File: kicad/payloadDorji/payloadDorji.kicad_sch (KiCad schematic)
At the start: 21 parts, among them J1 Conn_01x01_Pin, J2 Conn_Coaxial, J3 Conn_01x06_Male, U1 LM386, U2 DRA818V, U3 STM32L432KCUx

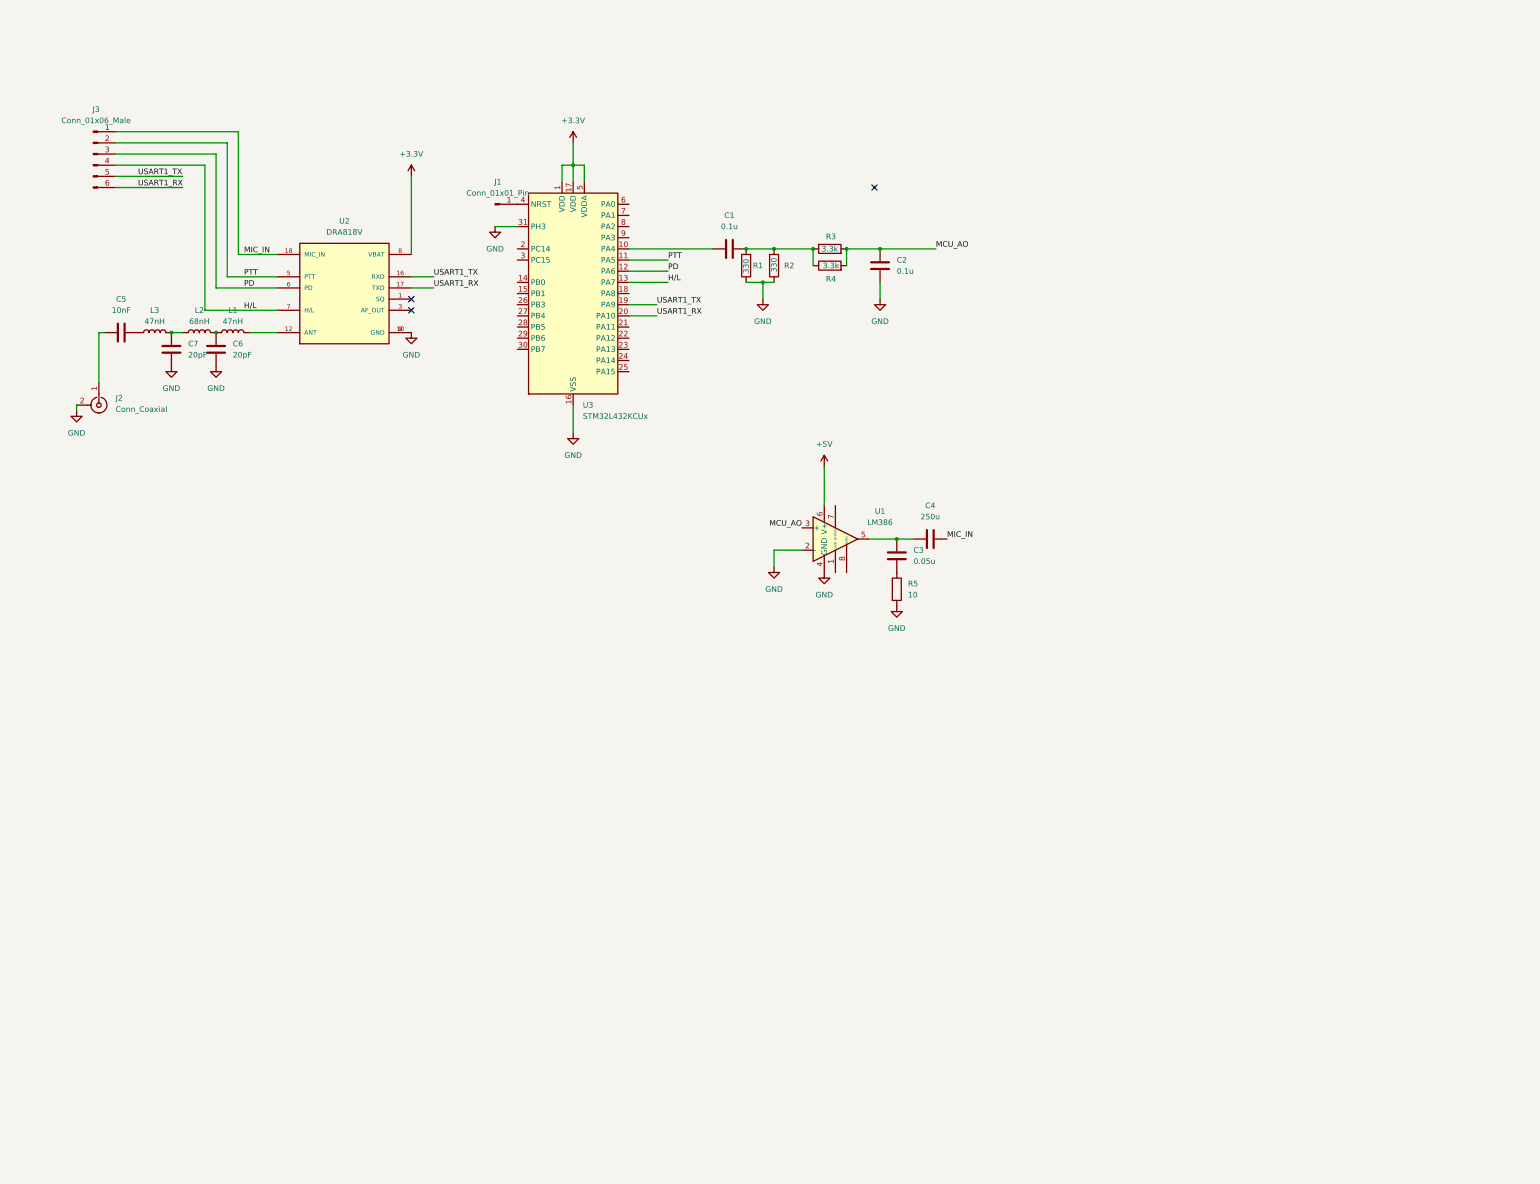
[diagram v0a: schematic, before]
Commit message: payloadDorji add gps and power
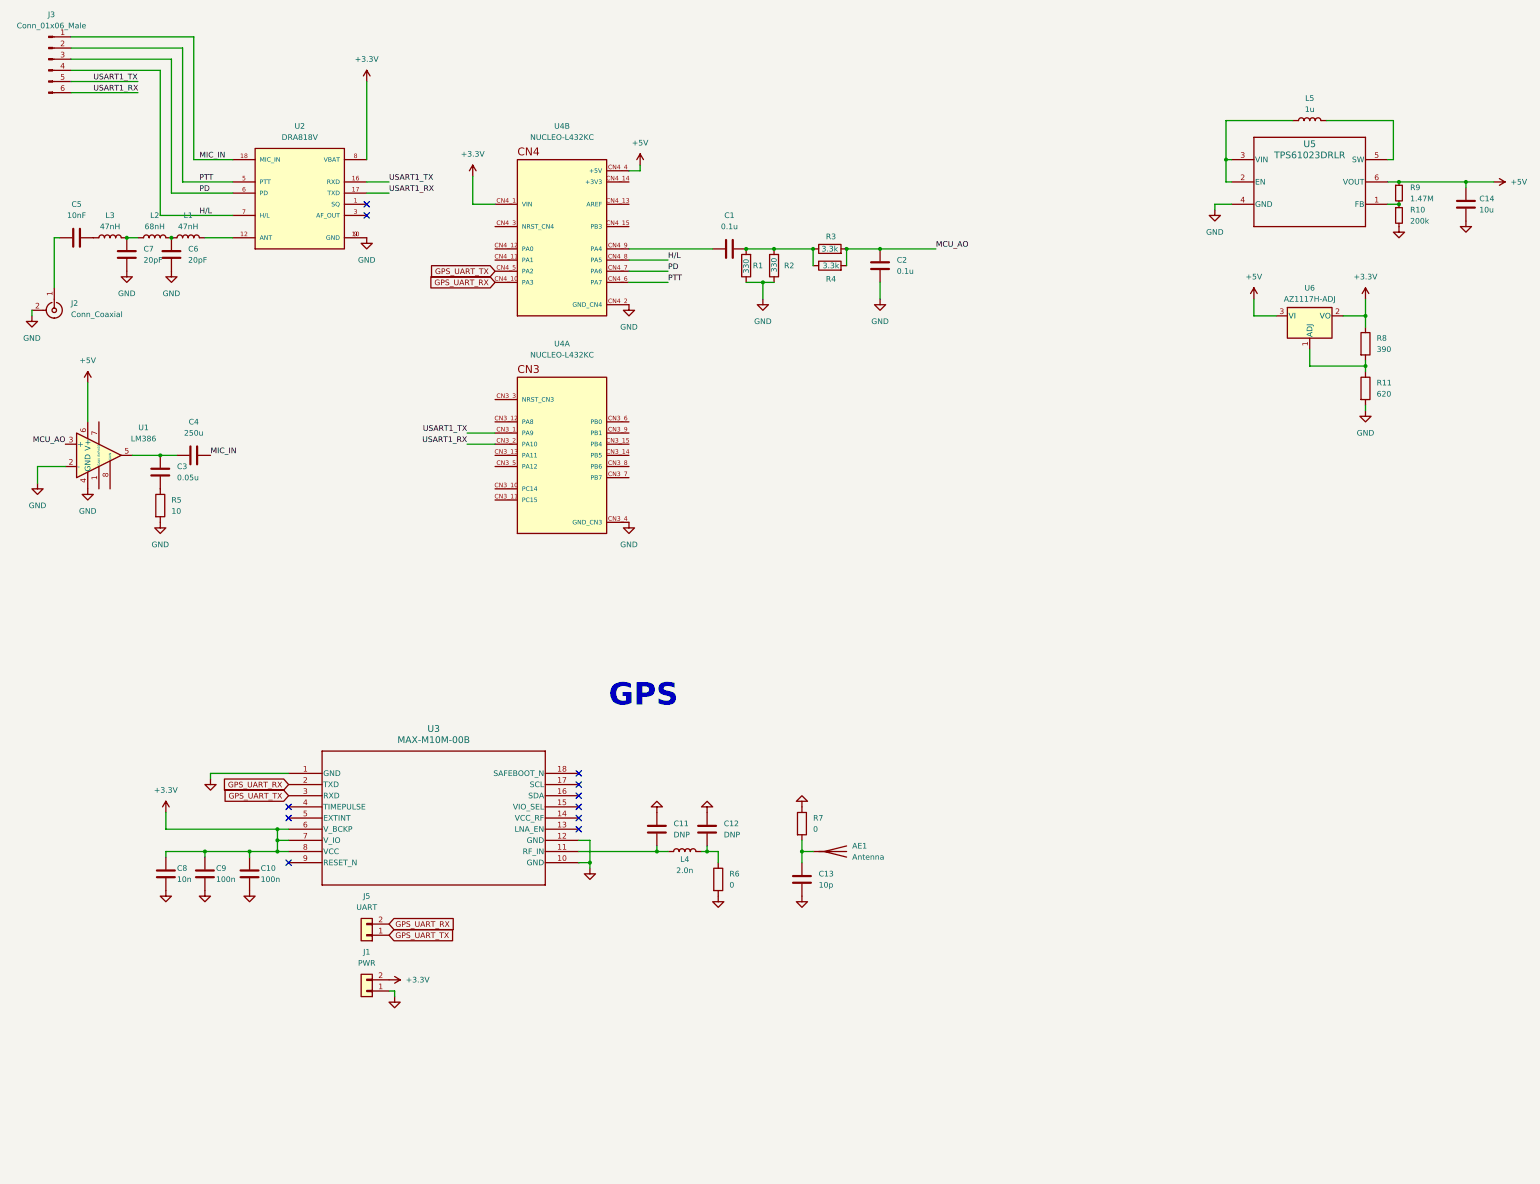
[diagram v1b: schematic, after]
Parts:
- removed J1: Conn_01x01_Pin, Connector_PinSocket_2.54mm:PinSocket_1x01_P2.54mm_Vertical, symbol Connector:Conn_01x01_Pin
- removed U3: STM32L432KCUx, Package_DFN_QFN:QFN-32-1EP_5x5mm_P0.5mm_EP3.45x3.45mm, symbol MCU_ST_STM32L4:STM32L432KCUx
- added AE1: Antenna, PicoAPRS-CustomFootprints:AC30157-01 GNSS Ceramic Chip, symbol Device:Antenna
- added C10, C9: 100n, Capacitor_SMD:C_0402_1005Metric, symbol Device:C
- added C11, C12: DNP, Capacitor_SMD:C_0603_1608Metric, symbol Device:C
- added C13: 10p, Capacitor_SMD:C_0603_1608Metric, symbol Device:C
- added C14: 10u, Capacitor_SMD:C_0603_1608Metric, symbol Device:C
- added C8: 10n, Capacitor_SMD:C_0402_1005Metric, symbol Device:C
- added J1: PWR, Connector_PinHeader_2.54mm:PinHeader_1x02_P2.54mm_Vertical, symbol Connector_Generic:Conn_01x02
- added J5: UART, Connector_PinHeader_2.54mm:PinHeader_1x02_P2.54mm_Vertical, symbol Connector_Generic:Conn_01x02
- added L4: 2.0n, Inductor_SMD:L_0603_1608Metric, symbol Device:L
- added L5: 1u, Inductor_SMD:L_0603_1608Metric, symbol Device:L
- added R10: 200k, Resistor_SMD:R_0603_1608Metric, symbol Device:R_Small
- added R11: 620, symbol Device:R
- added R6, R7: 0, Resistor_SMD:R_0603_1608Metric, symbol Device:R
- added R8: 390, symbol Device:R
- added R9: 1.47M, Resistor_SMD:R_0603_1608Metric, symbol Device:R_Small
- added U3: MAX-M10M-00B, PicoAPRS Custom Parts:MOD18_MAX-M10M_UBL, symbol MAX-M10M:MAX-M10M-00B
- added U4: NUCLEO-L432KC, NUCLEO-L432KC:MODULE_NUCLEO-L432KC, symbol NUCLEO-L432KC:NUCLEO-L432KC
- added U5: TPS61023DRLR, DRL0006A, symbol TPS61023:TPS61023DRLR
- added U6: AZ1117H-ADJ, Package_TO_SOT_SMD:SOT-223-3_TabPin2, symbol Regulator_Linear:AZ1117H-ADJ
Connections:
- net +3.3V: now also C10.1, C8.1, C9.1, J1.2 (Pin_2), R8.1, U3.6 (V_BCKP), U3.7 (V_IO), U3.8 (VCC), U4.CN4_1 (VIN), U6.2 (VO)
- net +5V: now also C14.1, R9.1, U4.CN4_4 (+5V), U5.6 (VOUT), U6.3 (VI)
- net GND: now also C10.2, C11.1, C12.1, C13.2, C14.2, C8.2, C9.2, J1.1 (Pin_1), R10.2, R11.2, R6.2, R7.1, U3.1 (GND), U3.10 (GND), U3.12 (GND), U4.CN3_4 (GND_CN3), U4.CN4_2 (GND_CN4), U5.4 (GND)
- net H/L: now also U4.CN4_8 (PA5)
- net PD: now also U4.CN4_7 (PA6)
- net PTT: now also U4.CN4_6 (PA7)
- net USART1_RX: now also U4.CN3_2 (PA10)
- net USART1_TX: now also U4.CN3_1 (PA9)
- net at C1.1: now also U4.CN4_9 (PA4)
- new net: L5.1, U5.2 (EN), U5.3 (VIN)
- new net: L5.2, U5.5 (SW)
- new net: C12.2, L4.1, R6.1
- new net: C11.2, L4.2, U3.11 (RF_IN)
- new net: R10.1, R9.2, U5.1 (FB)
- new net: AE1.1 (A), C13.1, R7.2
- new net: R11.1, R8.2, U6.1 (ADJ)
- new net GPS_UART_RX: J5.2 (Pin_2), U3.2 (TXD), U4.CN4_10 (PA3)
- new net GPS_UART_TX: J5.1 (Pin_1), U3.3 (RXD), U4.CN4_5 (PA2)
- no-connect marks 3 -> 11
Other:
- note added: "GPS"
- moved on the sheet: C3, C4, C5, C6, C7, J2, J3, L1, L2, L3, R5, U1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

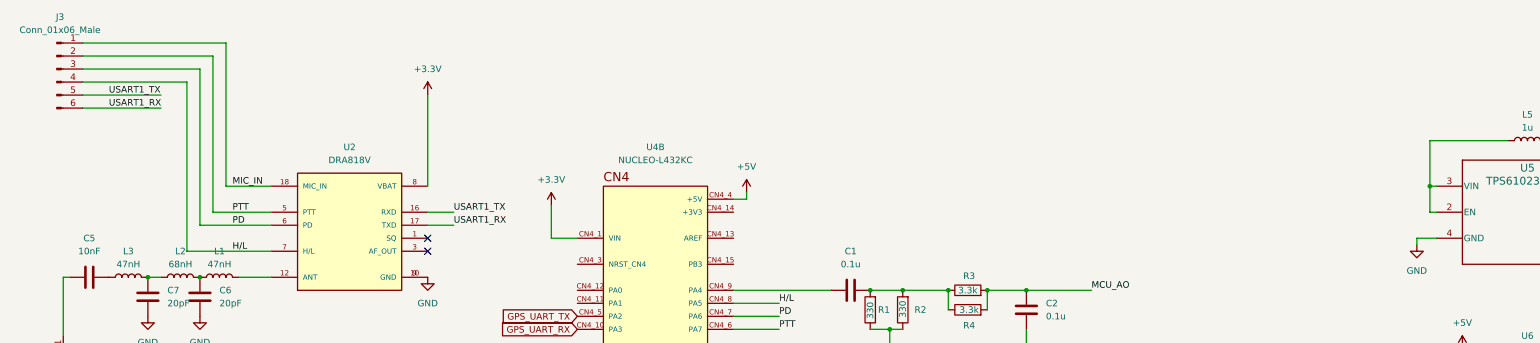
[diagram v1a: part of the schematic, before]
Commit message: payloadDorji add gps and power
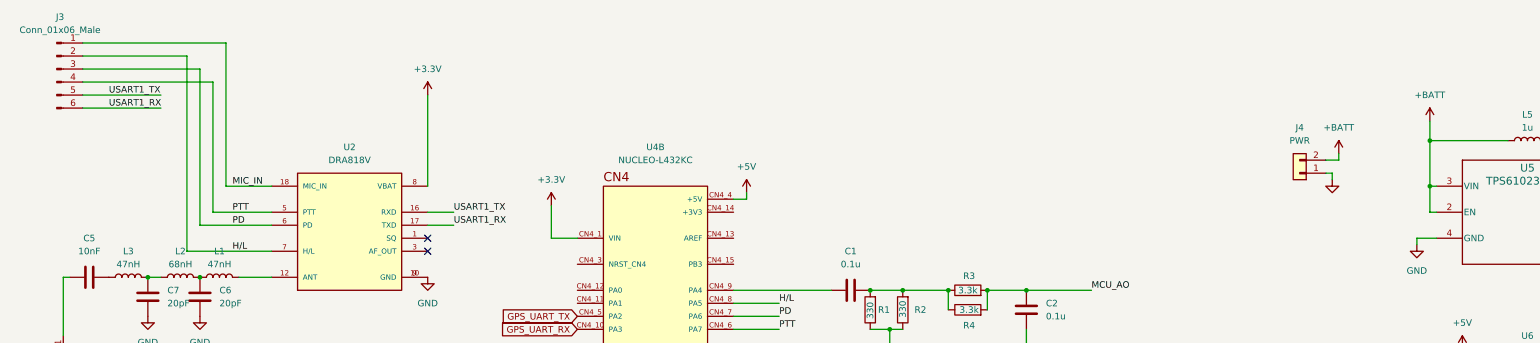
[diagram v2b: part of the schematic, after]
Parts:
- added J4: PWR, Connector_PinHeader_2.54mm:PinHeader_1x02_P2.54mm_Vertical, symbol Connector_Generic:Conn_01x02
- R11, R8: footprint (none) -> Resistor_SMD:R_0603_1608Metric
- U2: footprint DRA818V:DORJI_DRA818V -> PicoAPRS-CustomFootprints:DORJI_DRA818V
- U3: footprint PicoAPRS Custom Parts:MOD18_MAX-M10M_UBL -> footprints:MOD18_MAX-M10M_UBL
- U5: footprint DRL0006A -> footprints:DRL0006A
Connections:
- net GND: now also J4.1 (Pin_1)
- net H/L: now also J3.2 (Pin_2); no longer J3.4 (Pin_4)
- net PTT: now also J3.4 (Pin_4); no longer J3.2 (Pin_2)
- net +BATT: now reaches L5.1, U5.2 (EN), U5.3 (VIN)
- net +BATT: now also J4.2 (Pin_2)

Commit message: some fixes, not done yet
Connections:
- net +3.3V: no longer U4.CN4_1 (VIN)
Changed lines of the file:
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@@
 	(wire
 		(pts
-			(xy 123.19 62.23) (xy 123.19 55.88)
-		)
-		(stroke
-			(width 0)
-			(type default)
-		)
-	)
-	(wire
-		(pts
 			(xy 24.13 121.92) (xy 30.48 121.92)
 		)
@@
 	(wire
 		(pts
-			(xy 128.27 62.23) (xy 123.19 62.23)
-		)
-		(stroke
-			(width 0)
-			(type default)
-		)
-	)
-	(wire
-		(pts
 			(xy 167.64 209.55) (xy 165.1 209.55)
 		)
@@
 					(unit 1)
 				)
-			)
-		)
-	)
-	(symbol
-		(lib_id "power:+3.3V")
-		(at 123.19 55.88 0)
-		(unit 1)
-		(exclude_from_sim no)
-		(in_bom yes)
-		(on_board yes)
-		(dnp no)
-		(fields_autoplaced yes)
-		(property "Reference" "#PWR03"
-			(at 123.19 59.69 0)
-			(effects
-				(font
-					(size 1.27 1.27)
-				)
-				(hide yes)
-			)
-		)
-		(property "Value" "+3.3V"
-			(at 123.19 50.8 0)
-			(effects
-				(font
-					(size 1.27 1.27)
-				)
-			)
-		)
-		(property "Footprint" ""
-			(at 123.19 55.88 0)
-			(effects
-				(font
-					(size 1.27 1.27)
-				)
-				(hide yes)
-			)
-		)
-		(property "Datasheet" ""
-			(at 123.19 55.88 0)
-			(effects
-				(font
-					(size 1.27 1.27)
-				)
-				(hide yes)
-			)
-		)
-		(property "Description" "Power symbol creates a global label with name \"+3.3V\""
-			(at 123.19 55.88 0)
-			(effects
-				(font
-					(size 1.27 1.27)
-				)
-				(hide yes)
-			)
-		)
-		(pin "1"
-		)
-		(instances
-			(project "payloadDorji"
-				(path "/a1fbba56-c12c-4711-9b0a-2692694797db"
-					(reference "#PWR03")
-					(unit 1)
-				)

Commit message: no blow up
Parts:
- added C15, C16: 22u, Capacitor_SMD:C_0603_1608Metric, symbol Device:C
- added C17: 1u, Capacitor_SMD:C_0603_1608Metric, symbol Device:C
- added C18: 100n, Capacitor_SMD:C_0603_1608Metric, symbol Device:C
- added C19: 10u, Capacitor_SMD:C_0603_1608Metric, symbol Device:C
- C10, C8, C9: footprint Capacitor_SMD:C_0402_1005Metric -> Capacitor_SMD:C_0603_1608Metric
- L5: footprint Inductor_SMD:L_0603_1608Metric -> Inductor_THT:L_Axial_L5.0mm_D3.6mm_P10.00mm_Horizontal_Murata_BL01RN1A2A2
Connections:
- net +3.3V: now also C16.1, C17.1, C18.1
- net +5V: now also C15.1
- net +BATT: now also C19.1
- net GND: now also C15.2, C16.2, C17.2, C18.2, C19.2

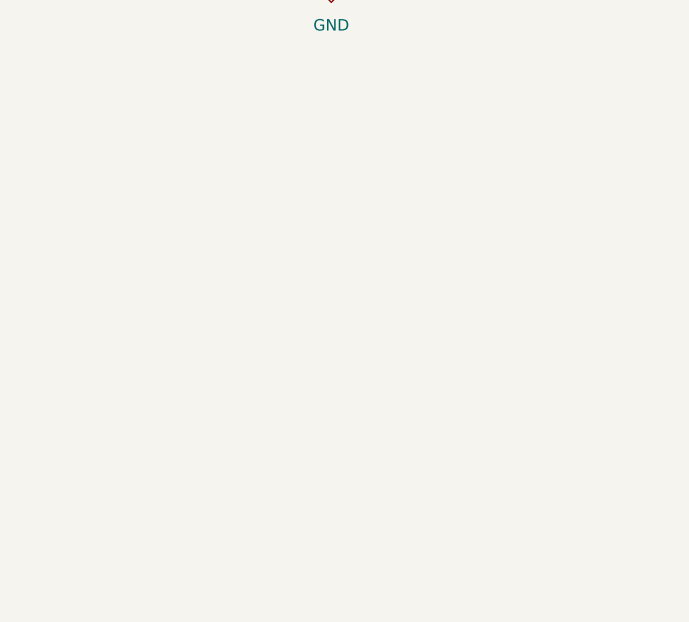
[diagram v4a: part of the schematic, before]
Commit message: mounting holes, vias, etc
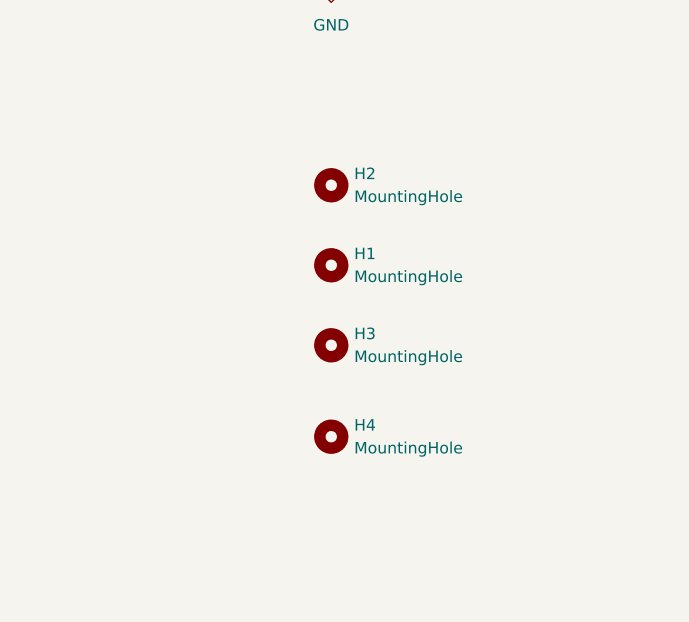
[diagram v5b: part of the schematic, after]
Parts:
- added H1, H2, H3, H4: MountingHole, symbol Mechanical:MountingHole
- L5: footprint Inductor_THT:L_Axial_L5.0mm_D3.6mm_P10.00mm_Horizontal_Murata_BL01RN1A2A2 -> Inductor_SMD:L_1008_2520Metric
